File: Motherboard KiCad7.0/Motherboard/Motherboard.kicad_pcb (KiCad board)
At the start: 2 copper layers, 83.8 x 83.8 mm, 93 parts, among them J1 USB_B_Micro, J10 430450200, J11 430450200, J12 430450200, J2 SWD_01x04_Pin, J3 430450200, J4 430450200, J5 B04B-XASK-1, J6 430450200, J7 430450200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

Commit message: Final Changes
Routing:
- net Net-(D1-DOUT): track 59.7 -> 65.5 mm
- net Net-(BZ1--): track 16.4 -> 17.0 mm
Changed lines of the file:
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@@
   (segment (start 206.75 121.605) (end 208.17 123.025) (width 0.3) (layer "F.Cu") (net 1))
   (segment (start 206.75 113.575) (end 206.75 115.55) (width 0.3) (layer "F.Cu") (net 1))
-  (segment (start 210.175 113.45) (end 210.15 113.475) (width 0.3) (layer "F.Cu") (net 2))
-  (segment (start 213.95 113.625) (end 213.775 113.45) (width 0.3) (layer "F.Cu") (net 2))
+  (segment (start 210.475 113.15) (end 210.15 113.475) (width 0.3) (layer "F.Cu") (net 2))
+  (segment (start 213.95 122.325) (end 213.95 113.625) (width 0.3) (layer "F.Cu") (net 2))
+  (segment (start 213.95 113.625) (end 213.475 113.15) (width 0.3) (layer "F.Cu") (net 2))
+  (segment (start 213.475 113.15) (end 210.475 113.15) (width 0.3) (layer "F.Cu") (net 2))
+  (segment (start 208.2 113.475) (end 210.525 113.475) (width 0.3) (layer "F.Cu") (net 2))
   (segment (start 210.525 113.475) (end 210.85 113.15) (width 0.3) (layer "F.Cu") (net 2))
-  (segment (start 208.2 113.475) (end 210.15 113.475) (width 0.3) (layer "F.Cu") (net 2))
   (segment (start 213.25 123.025) (end 213.95 122.325) (width 0.3) (layer "F.Cu") (net 2))
   (segment (start 210.15 113.475) (end 210.525 113.475) (width 0.3) (layer "F.Cu") (net 2))
-  (segment (start 213.95 122.325) (end 213.95 113.625) (width 0.3) (layer "F.Cu") (net 2))
-  (segment (start 213.775 113.45) (end 210.175 113.45) (width 0.3) (layer "F.Cu") (net 2))
   (segment (start 195.825 139.725) (end 195.225 140.325) (width 0.3) (layer "F.Cu") (net 3))
   (segment (start 190.725 133.7625) (end 190.575 133.9125) (width 0.3) (layer "F.Cu") (net 3))
@@
   (segment (start 194.2 138.775) (end 195.65 138.775) (width 0.3) (layer "B.Cu") (net 3))
   (segment (start 196.4 139.625) (end 197 140.225) (width 0.3) (layer "B.Cu") (net 3))
+  (segment (start 174.290241 100.575) (end 173.765241 100.05) (width 0.2) (layer "F.Cu") (net 4))
   (segment (start 192.875 154.825) (end 192.875 155.925) (width 0.5) (layer "F.Cu") (net 4))
   (segment (start 178.545 136.85) (end 178.375 136.85) (width 0.3) (layer "F.Cu") (net 4))
@@
   (segment (start 185.6 122.059) (end 185.6 124.125) (width 0.5) (layer "F.Cu") (net 4))
   (segment (start 177.012134 129.511396) (end 176.8 129.72353) (width 0.3) (layer "F.Cu") (net 4))
+  (segment (start 174.825 100.575) (end 174.290241 100.575) (width 0.2) (layer "F.Cu") (net 4))
   (segment (start 187.45 138.325) (end 187.45 137.273685) (width 0.3) (layer "F.Cu") (net 4))
   (segment (start 184.948675 132.198675) (end 184.430417 131.680417) (width 0.3) (layer "F.Cu") (net 4))
@@
   (segment (start 201.45 131.7) (end 202.424998 131.7) (width 0.5) (layer "F.Cu") (net 4))
   (segment (start 209.85 138.875) (end 210.1125 138.6125) (width 0.3) (layer "F.Cu") (net 4))
-  (segment (start 174.5 100.525) (end 174.5 101.4) (width 0.3) (layer "F.Cu") (net 4))
   (segment (start 210.1125 139.6625) (end 210.1 139.675) (width 0.3) (layer "F.Cu") (net 4))
   (segment (start 165.9 111.475) (end 165.975 111.55) (width 0.5) (layer "F.Cu") (net 4))
@@
   (segment (start 190.775 151.475) (end 190.825 151.525) (width 0.5) (layer "F.Cu") (net 4))
   (segment (start 189.775 126.2) (end 190.1 126.2) (width 0.5) (layer "F.Cu") (net 4))
-  (segment (start 174 100.025) (end 174.5 100.525) (width 0.3) (layer "F.Cu") (net 4))
   (segment (start 207.425 133.375) (end 208.525 132.275) (width 0.5) (layer "F.Cu") (net 4))
   (segment (start 209.625 140.15) (end 210.1 139.675) (width 0.5) (layer "F.Cu") (net 4))
@@
   (via (at 202.449998 131.725) (size 0.6) (drill 0.3) (layers "F.Cu" "B.Cu") (net 4))
   (via (at 210.1 139.675) (size 0.6) (drill 0.3) (layers "F.Cu" "B.Cu") (net 4))
+  (via (at 173.765241 100.05) (size 0.6) (drill 0.3) (layers "F.Cu" "B.Cu") (net 4))
   (via (at 213.875 109.875) (size 0.6) (drill 0.3) (layers "F.Cu" "B.Cu") (net 4))
   (via (at 211.675 136) (size 0.6) (drill 0.3) (layers "F.Cu" "B.Cu") (net 4))
@@
   (via (at 188.725 127.25) (size 0.6) (drill 0.3) (layers "F.Cu" "B.Cu") (net 4))
   (via (at 175.211127 129.615548) (size 0.6) (drill 0.3) (layers "F.Cu" "B.Cu") (net 4))
-  (via (at 174 100.025) (size 0.6) (drill 0.3) (layers "F.Cu" "B.Cu") (net 4))
   (via (at 180.25 138.875) (size 0.6) (drill 0.3) (layers "F.Cu" "B.Cu") (free) (net 4))
   (via (at 202.65 136.125) (size 0.6) (drill 0.3) (layers "F.Cu" "B.Cu") (net 4))
@@
   (segment (start 192.291 123.359) (end 192.325 123.325) (width 0.3) (layer "B.Cu") (net 45))
   (segment (start 186.9 123.375) (end 188.625 123.375) (width 0.3) (layer "B.Cu") (net 45))
-  (segment (start 216.18 99.28) (end 215.975 99.075) (width 0.5) (layer "F.Cu") (net 58))
+  (segment (start 216.75 99.05) (end 218.375 97.425) (width 0.5) (layer "F.Cu") (net 58))
   (segment (start 219.335 102.21) (end 219.775 102.65) (width 0.5) (layer "F.Cu") (net 58))
   (segment (start 218.375 95.95) (end 218.95 95.375) (width 0.5) (layer "F.Cu") (net 58))
+  (segment (start 216.275 99.05) (end 216.75 99.05) (width 0.5) (layer "F.Cu") (net 58))
+  (segment (start 216.18 102.21) (end 216.18 99.145) (width 0.5) (layer "F.Cu") (net 58))
   (segment (start 218.375 97.425) (end 218.375 95.95) (width 0.5) (layer "F.Cu") (net 58))
   (segment (start 216.18 102.21) (end 219.335 102.21) (width 0.5) (layer "F.Cu") (net 58))
-  (segment (start 215.975 99.075) (end 216.725 99.075) (width 0.5) (layer "F.Cu") (net 58))
-  (segment (start 216.725 99.075) (end 218.375 97.425) (width 0.5) (layer "F.Cu") (net 58))
-  (segment (start 216.18 102.21) (end 216.18 99.28) (width 0.5) (layer "F.Cu") (net 58))
+  (segment (start 216.18 99.145) (end 216.275 99.05) (width 0.5) (layer "F.Cu") (net 58))
   (segment (start 173.687278 130.124118) (end 174.2 129.611396) (width 0.3) (layer "F.Cu") (net 59))
   (segment (start 172.225 130.974937) (end 172.225 131.225) (width 0.3) (layer "F.Cu") (net 59))
@@
   (via (at 189.2 140.425) (size 0.6) (drill 0.3) (layers "F.Cu" "B.Cu") (net 61))
   (via (at 183.15 105.675) (size 0.6) (drill 0.3) (layers "F.Cu" "B.Cu") (net 61))
+  (segment (start 173.275 105.7) (end 173.3 105.675) (width 0.3) (layer "B.Cu") (net 61))
+  (segment (start 183.45 135.2) (end 182.15 133.9) (width 0.3) (layer "B.Cu") (net 61))
   (segment (start 185.625 138.15) (end 183.45 135.975) (width 0.3) (layer "B.Cu") (net 61))
+  (segment (start 183.45 135.975) (end 183.45 135.2) (width 0.3) (layer "B.Cu") (net 61))
   (segment (start 189.2 138.15) (end 185.625 138.15) (width 0.3) (layer "B.Cu") (net 61))
+  (segment (start 176.033769 125.896021) (end 173.275 123.137252) (width 0.3) (layer "B.Cu") (net 61))
+  (segment (start 189.2 140.425) (end 189.2 138.15) (width 0.3) (layer "B.Cu") (net 61))
+  (segment (start 182.15 131.1) (end 176.946021 125.896021) (width 0.3) (layer "B.Cu") (net 61))
+  (segment (start 173.275 123.137252) (end 173.275 105.7) (width 0.3) (layer "B.Cu") (net 61))
+  (segment (start 173.3 105.675) (end 183.15 105.675) (width 0.3) (layer "B.Cu") (net 61))
+  (segment (start 182.15 133.9) (end 182.15 131.1) (width 0.3) (layer "B.Cu") (net 61))
   (segment (start 176.946021 125.896021) (end 176.033769 125.896021) (width 0.3) (layer "B.Cu") (net 61))
-  (segment (start 176.033769 125.896021) (end 173.275 123.137252) (width 0.3) (layer "B.Cu") (net 61))
-  (segment (start 173.275 123.137252) (end 173.275 115.55) (width 0.3) (layer "B.Cu") (net 61))
-  (segment (start 182.15 131.1) (end 176.946021 125.896021) (width 0.3) (layer "B.Cu") (net 61))
-  (segment (start 173.275 115.55) (end 183.15 105.675) (width 0.3) (layer "B.Cu") (net 61))
-  (segment (start 183.45 135.2) (end 182.15 133.9) (width 0.3) (layer "B.Cu") (net 61))
-  (segment (start 189.2 140.425) (end 189.2 138.15) (width 0.3) (layer "B.Cu") (net 61))
-  (segment (start 182.15 133.9) (end 182.15 131.1) (width 0.3) (layer "B.Cu") (net 61))
-  (segment (start 183.45 135.975) (end 183.45 135.2) (width 0.3) (layer "B.Cu") (net 61))
   (segment (start 188.35 142.6) (end 189.175 141.775) (width 0.3) (layer "F.Cu") (net 63))
   (segment (start 186.875 142.6) (end 188.35 142.6) (width 0.3) (layer "F.Cu") (net 63))

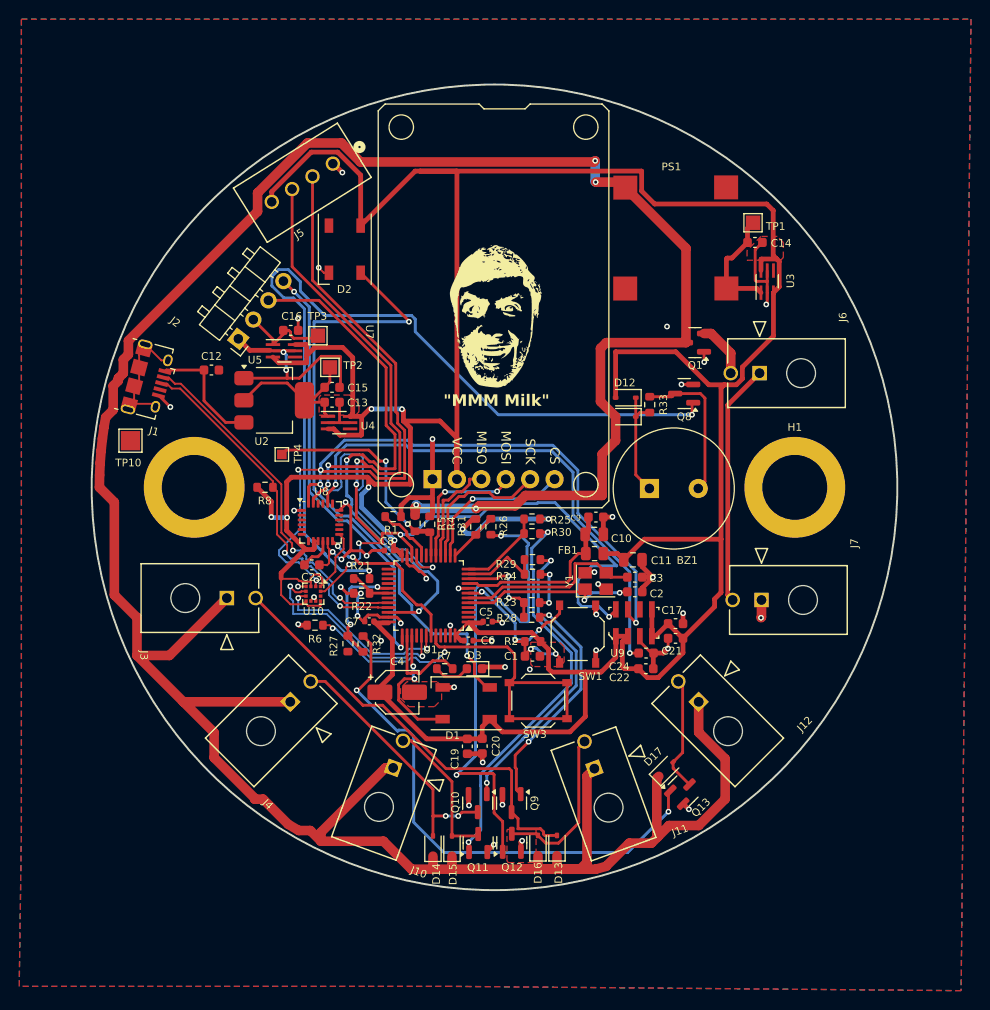
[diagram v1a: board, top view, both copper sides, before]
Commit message: Fixed AO444&A footprint
Fixed AO444&A footprint and symbol
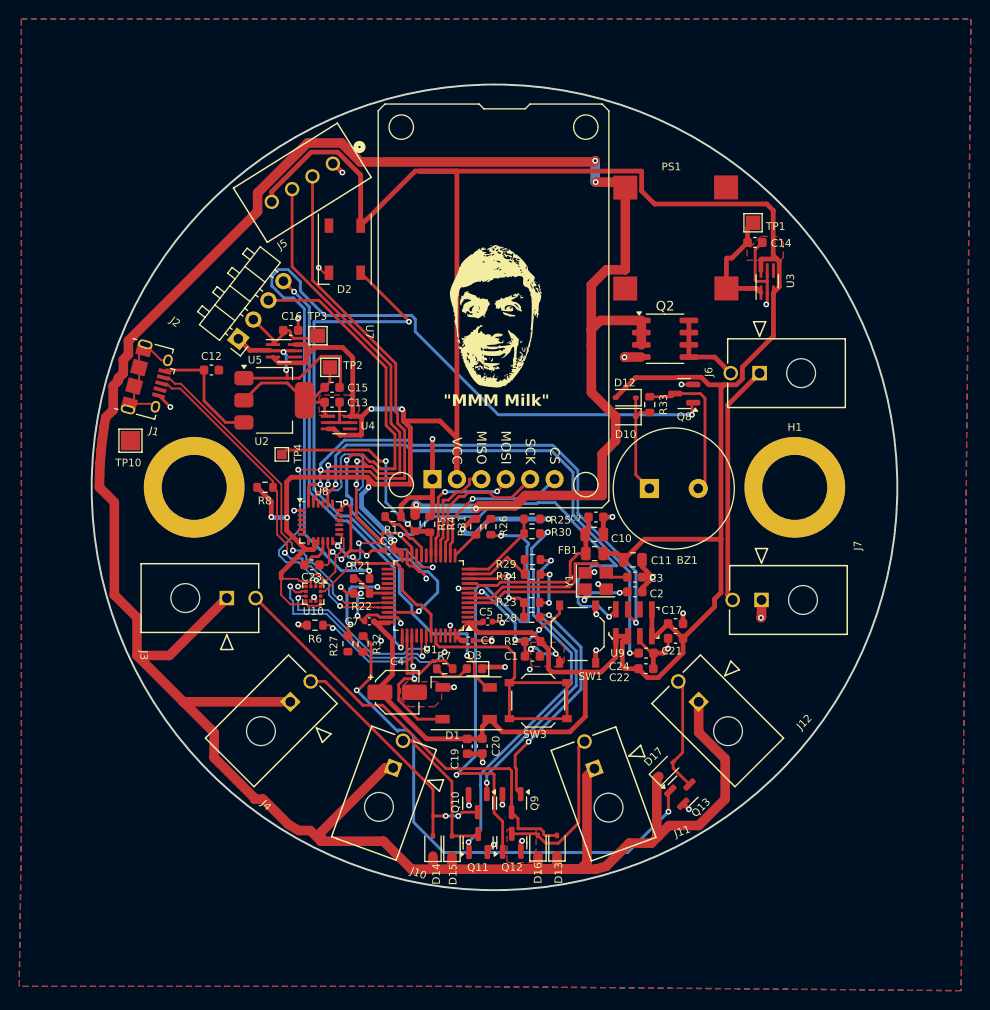
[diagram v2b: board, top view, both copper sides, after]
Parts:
- removed Q1: AO4447A, Package_TO_SOT_SMD:SOT-23
- added Q2: AO4447A, Package_SO:SOIC-8_3.9x4.9mm_P1.27mm, F.Cu at (209.8, 107.4)
- R7: value 560 -> 680
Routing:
- net +3.3V: track 386.8 -> 381.8 mm
- net Net-(J6-Pad2): track 5.71 -> 8.86 mm
- net GND: track 150.4 -> 151.1 mm, vias 51 -> 50

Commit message: Schematic and layout changes
Rewired ADCs
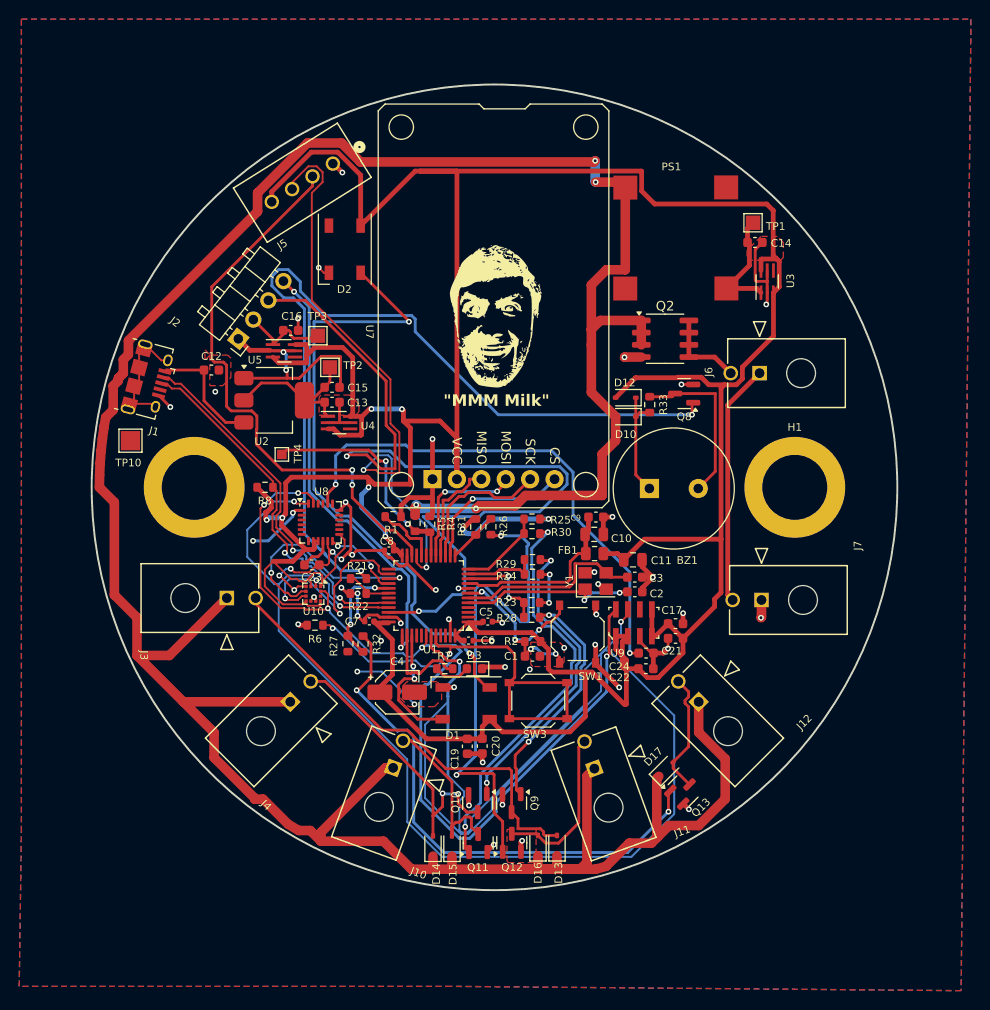
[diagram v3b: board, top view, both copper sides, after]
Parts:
- moved R21 0.35 mm to (177.9, 133.9)
- moved R22 0.32 mm to (177.9, 132.4)
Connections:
- U1 pad 21: SDA -> SCL
- U1 pad 22: SCL -> SDA
- U1 pad 26: unconnected-(U1-PB13-Pad26) -> ACCEL_INT2
- U1 pad 27: unconnected-(U1-PB14-Pad27) -> ACCEL_INT1
- U1 pad 28: unconnected-(U1-PB15-Pad28) -> GYRO_INT
- U1 pad 41: ACCEL_INT1 -> unconnected-(U1-PB5-Pad41)
- U1 pad 42: ACCEL_INT2 -> SCL_LOC
- U1 pad 43: GYRO_INT -> SDA_LOC
- U10 pad 12: SCL -> SCL_LOC
- U10 pad 2: SDA -> SDA_LOC
- U8 pad 23: SCL -> SCL_LOC
- U8 pad 24: SDA -> SDA_LOC
- U9 pad 7: SDA -> SDA_LOC
- U9 pad 8: SCL -> SCL_LOC
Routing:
- net SDA_LOC: track 0.00 -> 199.4 mm, vias 0 -> 4
- net SCL_LOC: track 0.00 -> 98.0 mm, vias 0 -> 5
- net SDA: track 144.0 -> 59.1 mm, vias 6 -> 2
- net SCL: track 111.8 -> 62.7 mm, vias 8 -> 2
- net SWDIO: track 56.7 -> 90.9 mm
- net GND: track 151.1 -> 180.6 mm, vias 50 -> 58
- net +3.3V: track 381.8 -> 395.2 mm
- net GYRO_INT: track 16.9 -> 8.22 mm
- net ACCEL_INT2: track 19.1 -> 22.9 mm
- net Net-(D14-A): track 27.0 -> 30.0 mm
- net Net-(D15-A): track 15.3 -> 17.9 mm
- net Net-(BZ1--): track 17.0 -> 18.8 mm
- net Net-(Q11-G): track 41.0 -> 42.2 mm
- net Sol_1: track 8.80 -> 7.73 mm
- net SWCLK: track 45.0 -> 46.1 mm
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
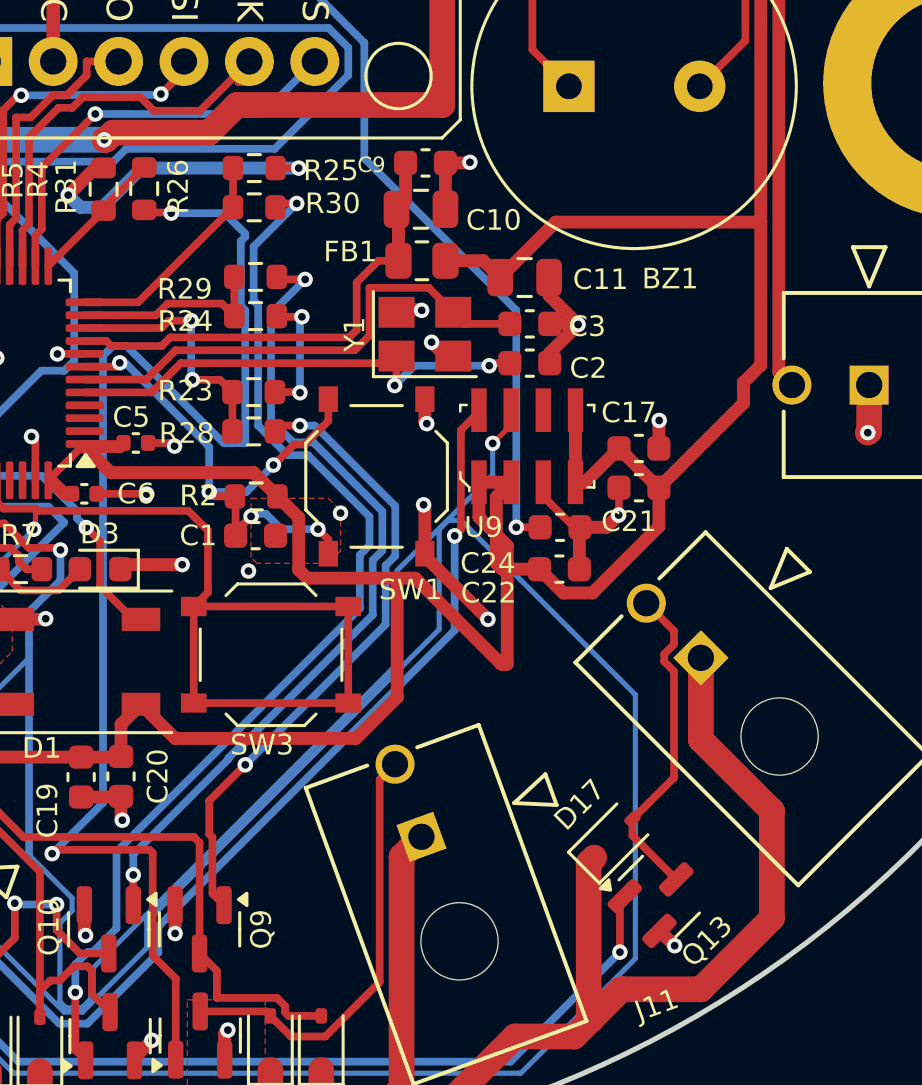
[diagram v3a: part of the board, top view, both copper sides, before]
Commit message: Added pull-up resistors to I2C
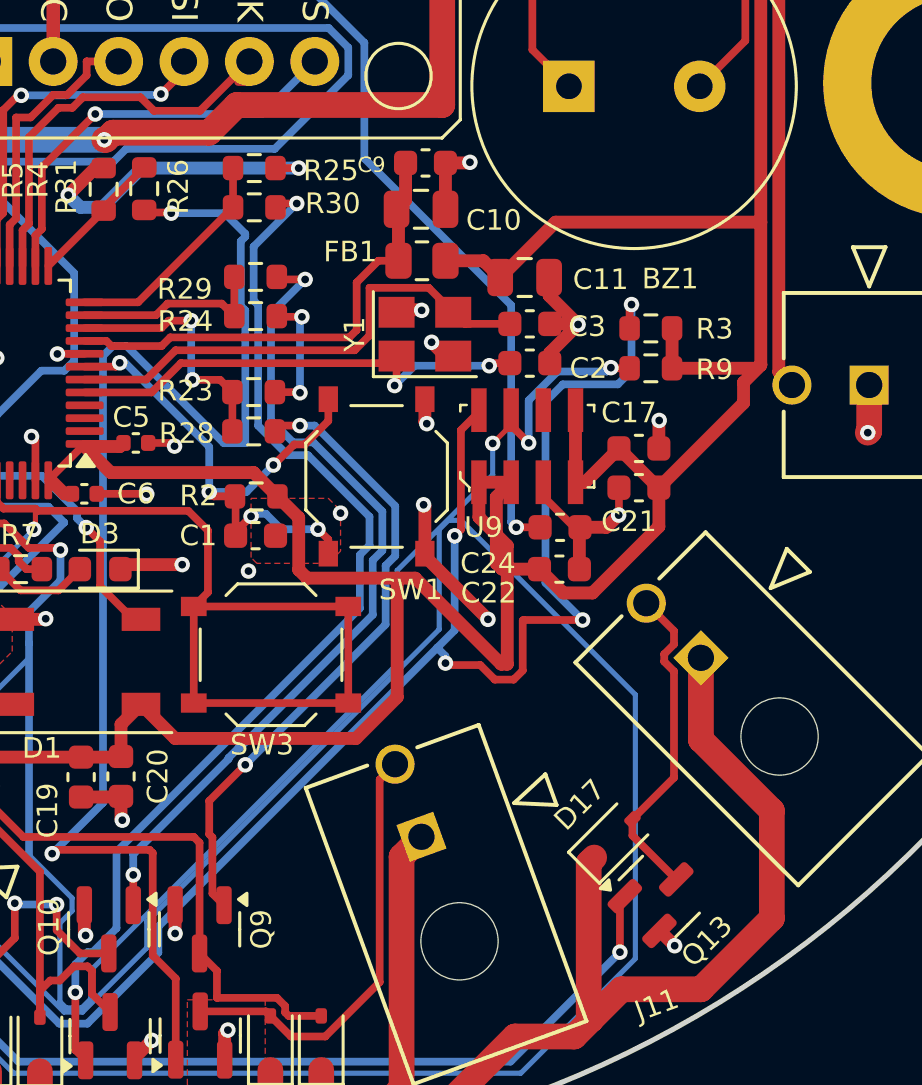
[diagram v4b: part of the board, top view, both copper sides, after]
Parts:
- added R3: 4.7k, Resistor_SMD:R_0603_1608Metric, F.Cu at (211.3, 132.4)
- added R9: 4.7k, Resistor_SMD:R_0603_1608Metric, F.Cu at (211.3, 134.0)
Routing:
- net SCL_LOC: track 98.0 -> 122.8 mm, vias 5 -> 8
- net SDA_LOC: track 199.4 -> 207.1 mm, vias 4 -> 6
- net +3.3V: track 395.2 -> 400.2 mm
